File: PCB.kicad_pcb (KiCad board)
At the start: 2 copper layers, 85 x 156.5 mm, 29 parts, among them J1 Conn_01x04, J2 Screw_Terminal_01x02, J3 Screw_Terminal_01x05, J4 Screw_Terminal_01x05, K1 G5LE-1A_DC3, K2 G5LE-1A_DC3, K3 G5LE-1, K4 G5LE-1, K6 G5LE-1, K7 G5LE-1A_DC3, Q1 DMN65D8L-7, Q2 DMN65D8L-7, Q3 DMN65D8L-7, SW2 SW_SPDT, SW3 Local DI2 (decspeed), SW4 local DI0 (onoff), SW5 Local DI1 (incspeed), U1 WeMos_D1_mini

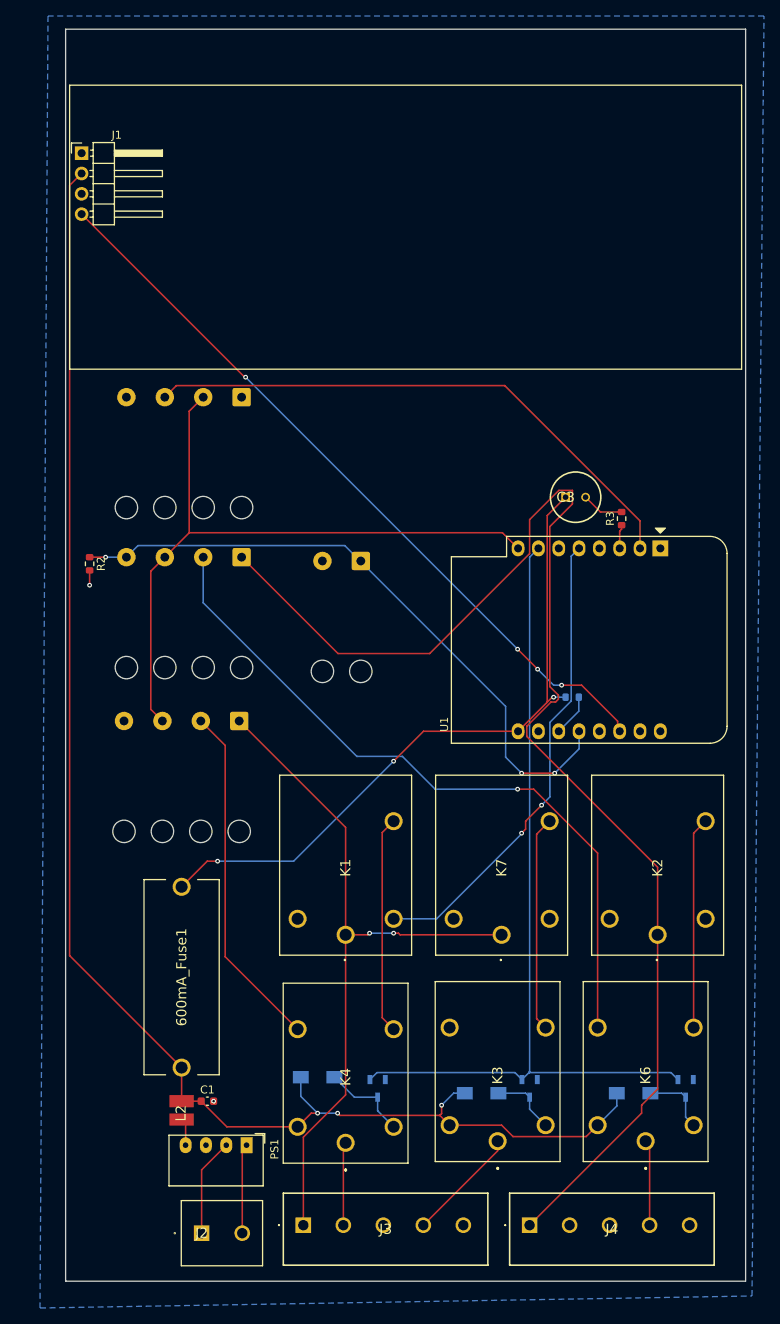
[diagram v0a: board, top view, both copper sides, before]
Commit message: remove the lots of vias so the layout is cleaner
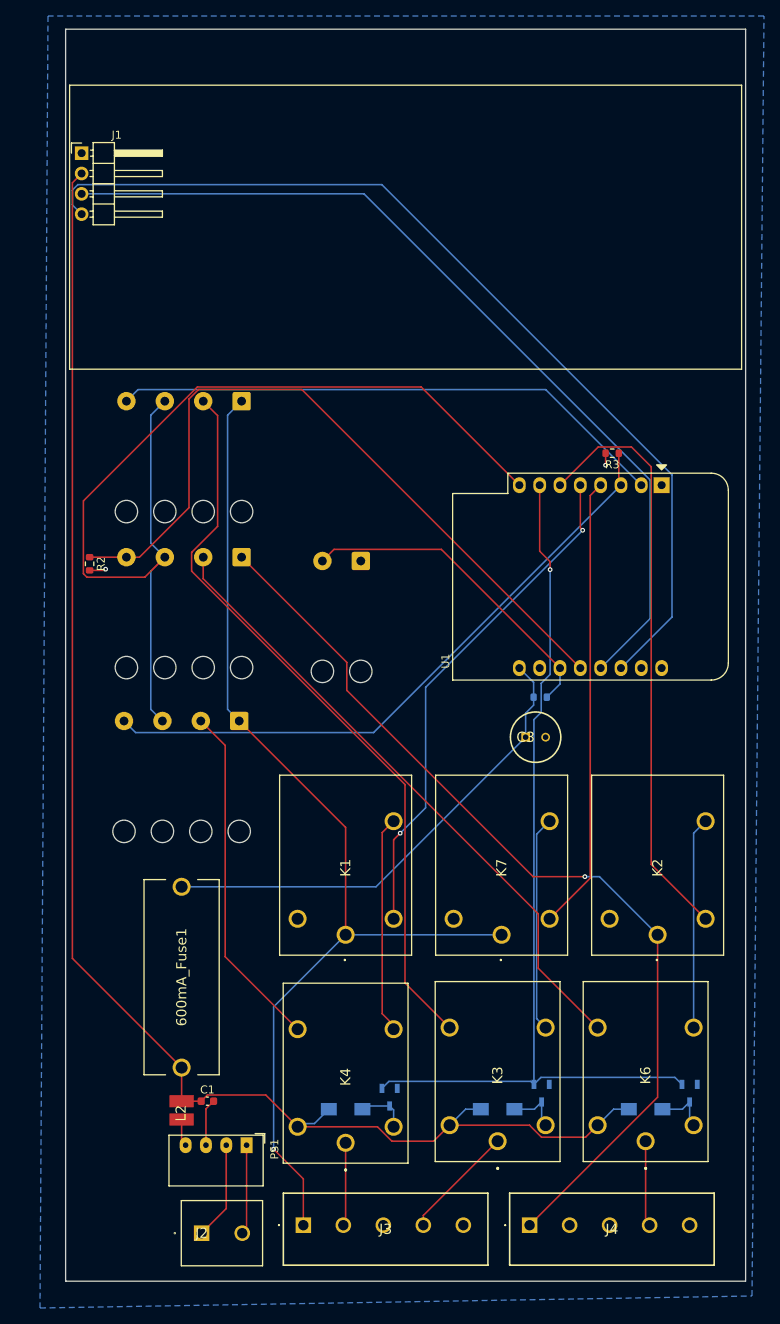
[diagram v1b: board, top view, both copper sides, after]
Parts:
- removed SW4: local DI0 (onoff), Connector_Wire:SolderWire-0.5sqmm_1x04_P4.8mm_D0.9mm_OD2.3mm_Relief
- added SW1: Local DI0 (onoff), Connector_Wire:SolderWire-0.5sqmm_1x04_P4.8mm_D0.9mm_OD2.3mm_Relief, B.Cu at (85.5, 111.5)
- SW2: value SW_SPDT -> local/remote switch
- moved C3 30.4 mm to (121.0, 153.5)
- moved R3 8.26 mm to (131.8, 118.0), turned to 180 degrees
- moved U1 7.90 mm to (138.0, 122.0)
- moved D2 5.32 mm to (98.5, 200.0)
- moved R1 4.00 mm to (122.8, 148.5)
- moved D1 2.83 mm to (117.5, 200.0)
- moved D3 2.50 mm to (136.0, 200.0)
- moved Q2 1.86 mm to (104.0, 198.5)
- moved Q1 1.62 mm to (123.0, 198.0)
- moved Q3 0.78 mm to (141.5, 198.0)
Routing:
- net SDA: track 0.00 -> 111.9 mm
- net local DI0: track 0.00 -> 93.8 mm
- net DO0: track 3.00 -> 79.6 mm
- net DO7: track 0.00 -> 73.7 mm
- net DO5: track 0.00 -> 56.8 mm
- net J4 24V: track 166.1 -> 116.5 mm, vias 0 -> 1
- net J3 24V: track 90.4 -> 134.6 mm, vias 2 -> 1
- net MCU 3V3: track 85.7 -> 128.7 mm
- net Net-(SW2-B): track 5.30 -> 40.8 mm
- net SCL: track 94.6 -> 120.5 mm, vias 4 -> 0
- net Net-(C3-+): track 84.4 -> 60.5 mm, vias 3 -> 0
- net DO3: track 80.7 -> 92.4 mm, vias 3 -> 0
- net local DI2: track 89.8 -> 79.2 mm, vias 1 -> 0
- net DO8: track 106.0 -> 115.0 mm, vias 0 -> 1
- net DO6: track 59.1 -> 64.1 mm
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
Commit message: update the pcb silkscreen names and start widening paths
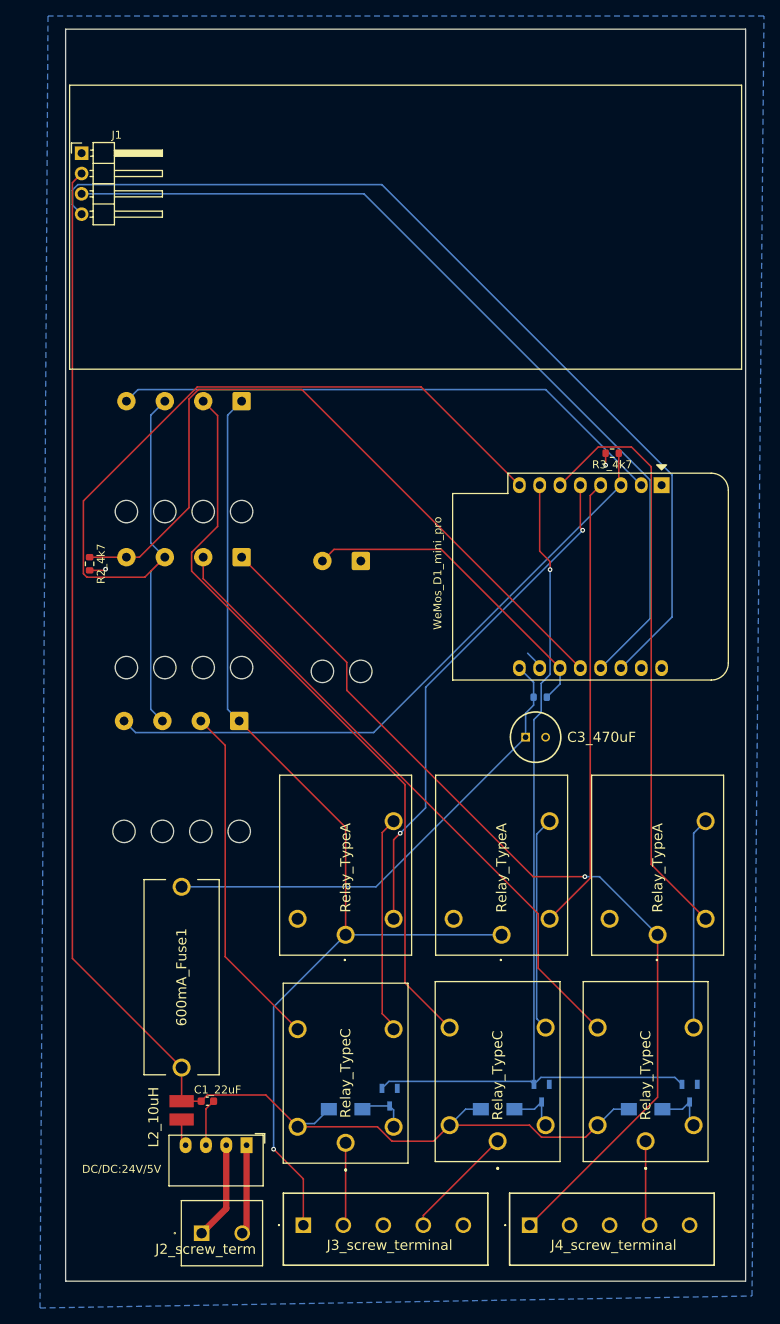
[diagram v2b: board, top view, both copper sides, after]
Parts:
- renumbered C1 to C1_22uF, C3 to C3_470uF, D1 to D1_Schottky, D2 to D2_Schottky, D3 to D3_Schottky, PS1 to DC/DC:24V/5V, J2 to J2_screw_term, J3 to J3_screw_terminal, J4 to J4_screw_terminal, L2 to L2_10uH, Q1 to Q1_MOSFET, Q2 to Q2_MOSFET, Q3 to Q3_MOSFET, R1 to R1_4k7, R2 to R2_4k7, R3 to R3_4k7, K7 to Relay_TypeA, K2 to Relay_TypeA, K1 to Relay_TypeA, K4 to Relay_TypeC, K3 to Relay_TypeC, K6 to Relay_TypeC, U1 to WeMos_D1_mini_pro
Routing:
- net GND: track 9.46 -> 11.9 mm
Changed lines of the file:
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@@
 		(descr "1729128")
 		(tags "Connector")
-		(property "Reference" "J2"
-			(at 0 0 0)
+		(property "Reference" "J2_screw_term"
+			(at 0.5 2 0)
 			(layer "F.SilkS")
 			(effects
@@
 		(descr "Resistor SMD 0603 (1608 Metric), square (rectangular) end terminal, IPC_7351 nominal, (Body size source: IPC-SM-782 page 72, https://www.pcb-3d.com/wordpress/wp-content/uploads/ipc-sm-782a_amendment_1_and_2.pdf), generated with kicad-footprint-generator")
 		(tags "resistor")
-		(property "Reference" "R3"
-			(at 0 -1.43 360)
+		(property "Reference" "R3_4k7"
+			(at 0 -1.43 0)
 			(layer "F.SilkS")
 			(effects
@@
 		)
 		(property "Value" "4k7"
-			(at 0 1.43 360)
+			(at 0 1.43 0)
 			(layer "F.Fab")
 			(effects
@@
 		)
 		(fp_text user "${REFERENCE}"
-			(at 0 0 360)
+			(at 0 0 0)
 			(layer "F.Fab")
 			(effects
@@
 		(descr "G5LE-1-DC3-1")
 		(tags "Relay or Contactor")
-		(property "Reference" "K4"
-			(at 8.225 0 90)
+		(property "Reference" "Relay_TypeC"
+			(at 8.7 0 90)
 			(layer "F.SilkS")
 			(effects
@@
 		)
 		(fp_text user "${REFERENCE}"
-			(at 8.225 0 90)
+			(at 8.7 0 90)
 			(layer "F.Fab")
 			(effects
@@
 		(descr "16-pin module, column spacing 22.86 mm (900 mils), https://wiki.wemos.cc/products:d1:d1_mini, https://c1.staticflickr.com/1/734/31400410271_f278b087db_z.jpg")
 		(tags "ESP8266 WiFi microcontroller")
-		(property "Reference" "U1"
-			(at 22 27 90)
+		(property "Reference" "WeMos_D1_mini_pro"
+			(at 11 28 90)
 			(layer "F.SilkS")
 			(effects
@@
 		)
 		(fp_text user "${REFERENCE}"
-			(at 11.43 10 90)
+			(at 11.43 10 180)
 			(layer "F.Fab")
 			(effects
@@
 		(descr "8200")
 		(tags "Inductor")
-		(property "Reference" "L2"
-			(at -0.37162 -0.07824 90)
+		(property "Reference" "L2_10uH"
+			(at -0.855 -3.5 90)
 			(layer "F.SilkS")
 			(effects
@@
 		)
 		(fp_text user "${REFERENCE}"
-			(at -0.37162 -0.07824 90)
+			(at -0.855 -3.5 90)
 			(layer "F.Fab")
 			(effects
@@
 		(descr "G5LE-1A4-DC5-4")
 		(tags "Relay or Contactor")
-		(property "Reference" "K7"
+		(property "Reference" "Relay_TypeA"
 			(at 8.375 0 90)
 			(layer "F.SilkS")
@@
 		(descr "6.3*11")
 		(tags "Capacitor Polarised")
-		(property "Reference" "C3"
-			(at 0 0 0)
+		(property "Reference" "C3_470uF"
+			(at 9.5 0 0)
 			(layer "F.SilkS")
 			(effects
@@
 		(descr "G5LE-1A4-DC5-4")
 		(tags "Relay or Contactor")
-		(property "Reference" "K2"
+		(property "Reference" "Relay_TypeA"
 			(at 8.375 0 90)
 			(layer "F.SilkS")
@@
 		(descr "1935190-1")
 		(tags "Connector")
-		(property "Reference" "J4"
-			(at 10.285 0.5 0)
+		(property "Reference" "J4_screw_terminal"
+			(at 10.5 2.5 0)
 			(layer "F.SilkS")
 			(effects
@@
 		)
 		(fp_text user "${REFERENCE}"
-			(at 10.285 0.5 0)
+			(at 10.5 2.5 0)
 			(layer "F.Fab")
 			(effects
@@
 		(descr "G5LE-1A4-DC5-4")
 		(tags "Relay or Contactor")
-		(property "Reference" "K1"
+		(property "Reference" "Relay_TypeA"
 			(at 8.375 0 90)
 			(layer "F.SilkS")
@@
 		(descr "Resistor SMD 0603 (1608 Metric), square (rectangular) end terminal, IPC_7351 nominal, (Body size source: IPC-SM-782 page 72, https://www.pcb-3d.com/wordpress/wp-content/uploads/ipc-sm-782a_amendment_1_and_2.pdf), generated with kicad-footprint-generator")
 		(tags "resistor")
-		(property "Reference" "R2"
+		(property "Reference" "R2_4k7"
 			(at 0 -1.43 90)
 			(layer "F.SilkS")
@@
 		(descr "Capacitor SMD 0603 (1608 Metric), square (rectangular) end terminal, IPC_7351 nominal, (Body size source: IPC-SM-782 page 76, https://www.pcb-3d.com/wordpress/wp-content/uploads/ipc-sm-782a_amendment_1_and_2.pdf), generated with kicad-footprint-generator")
 		(tags "capacitor")
-		(property "Reference" "C1"
-			(at 0 -1.43 0)
+		(property "Reference" "C1_22uF"
+			(at 1.275 -1.43 0)
 			(layer "F.SilkS")
 			(effects
@@
 		(descr "G5LE-1-DC3-1")
 		(tags "Relay or Contactor")
-		(property "Reference" "K3"
+		(property "Reference" "Relay_TypeC"
 			(at 8.225 0 90)
 			(layer "F.SilkS")
@@
 		(descr "http://power.murata.com/data/power/ncl/kdc_cre1.pdf")
 		(tags "murata dc-dc transformer")
-		(property "Reference" "PS1"
-			(at 0.5 -3.5 90)
+		(property "Reference" "DC/DC:24V/5V"
+			(at 3 15.62 360)
 			(layer "F.SilkS")
 			(effects
@@
 		(descr "G5LE-1-DC3-1")
 		(tags "Relay or Contactor")
-		(property "Reference" "K6"
+		(property "Reference" "Relay_TypeC"
 			(at 8.225 0 90)
 			(layer "F.SilkS")
@@
 		(descr "1935190-1")
 		(tags "Connector")
-		(property "Reference" "J3"
-			(at 10.285 0.5 0)
+		(property "Reference" "J3_screw_terminal"
+			(at 10.785 2.5 0)
 			(layer "F.SilkS")
 			(effects
@@
 		)
 		(fp_text user "${REFERENCE}"
-			(at 10.285 0.5 0)
+			(at 10.785 2.5 0)
 			(layer "F.Fab")
 			(effects
@@
 		(descr "DMN65D8L-7")
 		(tags "MOSFET (N-Channel)")
-		(property "Reference" "Q3"
-			(at 0 0 90)
+		(property "Reference" "Q3_MOSFET"
+			(at 0 -3 90)
 			(layer "B.SilkS")
 			(effects
@@
 		)
 		(fp_text user "${REFERENCE}"
-			(at 0 0 90)
+			(at 0 -3 90)
 			(layer "B.Fab")
 			(effects
@@
 		(descr "DMN65D8L-7")
 		(tags "MOSFET (N-Channel)")
-		(property "Reference" "Q2"
-			(at 0 0 90)
+		(property "Reference" "Q2_MOSFET"
+			(at 0 -3 90)
 			(layer "B.SilkS")
 			(effects
@@
 		)
 		(fp_text user "${REFERENCE}"
-			(at 0 0 90)
+			(at 0 -3 90)
 			(layer "B.Fab")
 			(effects
@@
 		(descr "DMN65D8L-7")
 		(tags "MOSFET (N-Channel)")
-		(property "Reference" "Q1"
-			(at 0 0 90)
+		(property "Reference" "Q1_MOSFET"
+			(at 0 -2 90)
 			(layer "B.SilkS")
 			(effects
@@
 		)
 		(fp_text user "${REFERENCE}"
-			(at 0 0 90)
+			(at 0 -2 90)
 			(layer "B.Fab")
 			(effects
@@
 		(descr "Resistor SMD 0603 (1608 Metric), square (rectangular) end terminal, IPC_7351 nominal, (Body size source: IPC-SM-782 page 72, https://www.pcb-3d.com/wordpress/wp-content/uploads/ipc-sm-782a_amendment_1_and_2.pdf), generated with kicad-footprint-generator")
 		(tags "resistor")
-		(property "Reference" "R1"
+		(property "Reference" "R1_4k7"
 			(at 0 1.43 0)
 			(layer "B.SilkS")
@@
 		)
 		(fp_text user "${REFERENCE}"
-			(at 0 0 0)
+			(at 2.675 -0.25 0)
 			(layer "B.Fab")
 			(effects
@@
 		(descr "SMA~DO-214AC")
 		(tags "Schottky Diode")
-		(property "Reference" "D2"
-			(at 0 0 0)
+		(property "Reference" "D2_Schottky"
+			(at -2 -2.5 0)
 			(layer "B.SilkS")
 			(effects
@@
 		(descr "SMA~DO-214AC")
 		(tags "Schottky Diode")
-		(property "Reference" "D3"
-			(at 0 0 0)
+		(property "Reference" "D3_Schottky"
+			(at -2.5 -2.5 0)
 			(layer "B.SilkS")
 			(effects
@@
 		(descr "SMA~DO-214AC")
 		(tags "Schottky Diode")
-		(property "Reference" "D1"
-			(at 0 0 0)
+		(property "Reference" "D1_Schottky"
+			(at -2 -2.5 0)
 			(layer "B.SilkS")
 			(effects
@@
 	)
 	(segment
-		(start 80.45 199)
-		(end 80.5 199)
-		(width 0.2)
-		(layer "F.Cu")
-		(net 1)
-	)
-	(segment
 		(start 121.484745 202)
 		(end 122.984745 203.5)
@@
 	)
 	(segment
+		(start 122.76 144.86)
+		(end 122.76 144.51)
+		(width 0.2)
+		(layer "B.Cu")
+		(net 2)
+	)
+	(segment
+		(start 122.76 144.51)
+		(end 121.25 143)
+		(width 0.2)
+		(layer "B.Cu")
+		(net 2)
+	)
+	(segment
 		(start 86.12 214.96)
 		(end 85.58 215.5)
@@
 		(start 86.12 204.5)
 		(end 86.12 214.96)
-		(width 0.2)
+		(width 0.8)
 		(layer "F.Cu")
 		(net 3)
@@
 		(start 83.58 204.5)
 		(end 83.58 212.42)
-		(width 0.2)
+		(width 0.8)
 		(layer "F.Cu")
 		(net 14)
@@
 		(start 83.58 212.42)
 		(end 80.5 215.5)
-		(width 0.2)
+		(width 0.8)
 		(layer "F.Cu")
 		(net 14)

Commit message: widen tracks with larger current and fix the local/remote switch footprint
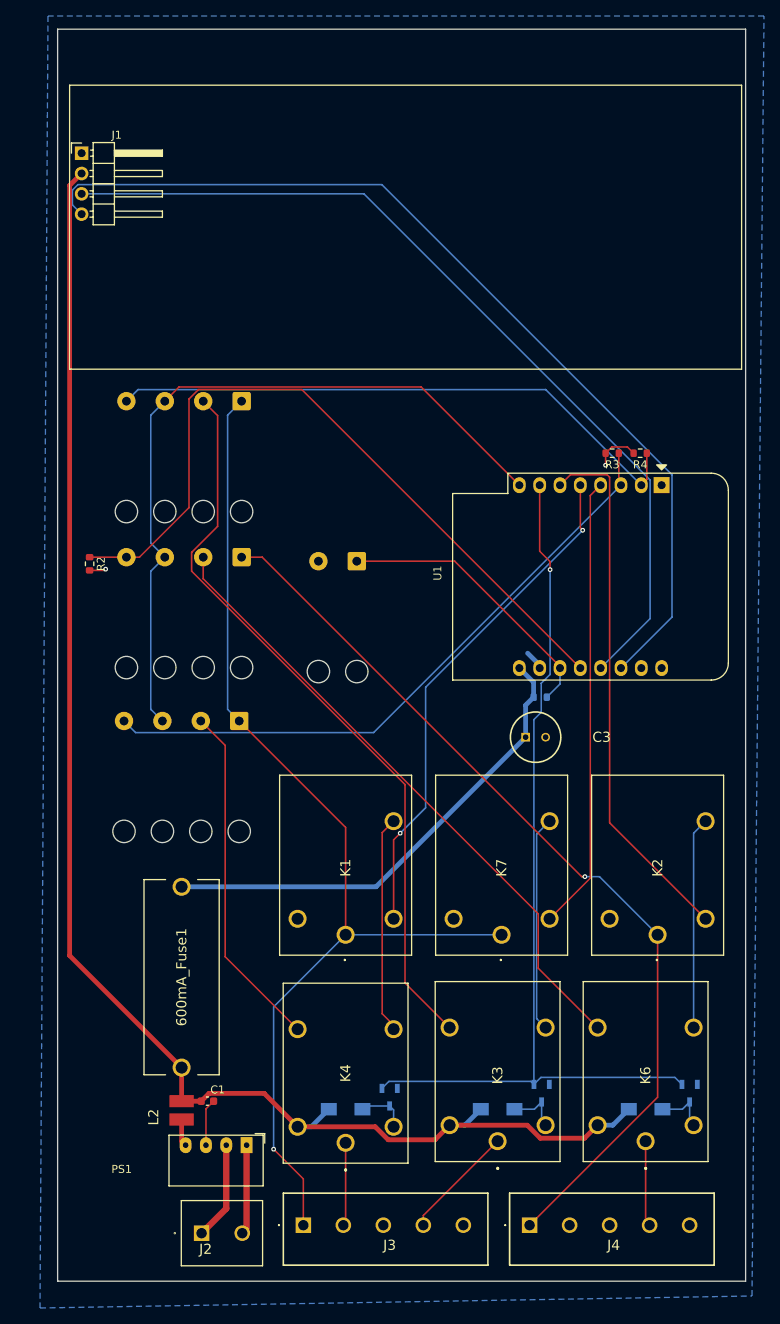
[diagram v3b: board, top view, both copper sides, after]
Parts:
- removed SW2: local/remote switch, Connector_Wire:SolderWire-0.5sqmm_1x02_P4.8mm_D0.9mm_OD2.3mm_Relief
- added R4: 4k7, Resistor_SMD:R_0603_1608Metric, F.Cu at (135.3, 118.0)
- added SW4: local/remote switch, Connector_Wire:SolderWire-0.5sqmm_1x02_P4.8mm_D0.9mm_OD2.3mm_Relief, B.Cu at (99.9, 131.5)
- renumbered C1_22uF to C1, C3_470uF to C3, D1_Schottky to D1, D2_Schottky to D2, D3_Schottky to D3, J2_screw_term to J2, J3_screw_terminal to J3, J4_screw_terminal to J4, Relay_TypeA to K1, Relay_TypeA to K2, Relay_TypeC to K3, Relay_TypeC to K4, Relay_TypeC to K6, Relay_TypeA to K7, L2_10uH to L2, DC/DC:24V/5V to PS1, Q1_MOSFET to Q1, Q2_MOSFET to Q2, Q3_MOSFET to Q3, R1_4k7 to R1, R2_4k7 to R2, R3_4k7 to R3, WeMos_D1_mini_pro to U1
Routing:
- net MCU 3V3: track 128.7 -> 92.9 mm
- net DO7: track 73.7 -> 67.0 mm
- net Net-(SW4-A): track 40.8 -> 35.4 mm
- net DOA: track 69.9 -> 74.2 mm
- net GND: track 11.9 -> 16.1 mm
- net J4 24V: track 116.5 -> 114.5 mm
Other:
- board size 85 x 156.5 mm -> 86 x 156.5 mm

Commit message: start improving the pcb schematic as per feedback no 2
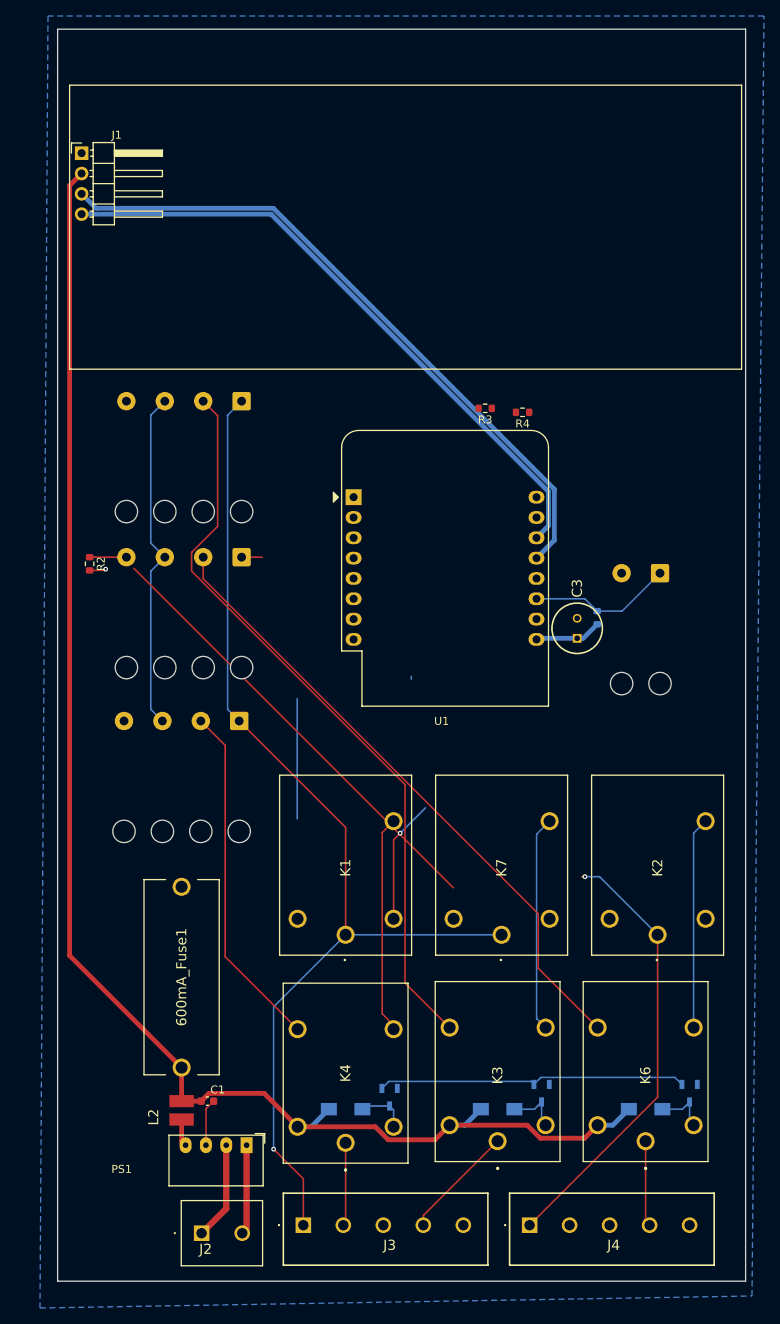
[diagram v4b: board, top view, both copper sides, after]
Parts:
- moved U1 38.5 mm to (99.5, 123.5), turned to 0 degrees
- moved SW4 37.9 mm to (137.8, 133.0)
- moved R3 16.8 mm to (115.9, 112.4)
- moved R4 15.6 mm to (120.6, 112.9)
- moved C3 13.9 mm to (127.4, 141.1), turned to 90 degrees
- moved R1 12.2 mm to (129.9, 138.6), turned to 90 degrees
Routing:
- net DO3: track 92.4 -> 4.60 mm
- net DO0: track 79.6 -> 0.00 mm
- net DO8: track 115.0 -> 38.7 mm, vias 1 -> 0
- net DOA: track 74.2 -> 0.00 mm
- net DO7: track 67.0 -> 0.00 mm
- net DO5: track 56.8 -> 0.00 mm
- net Net-(C3-+): track 60.5 -> 8.37 mm
- net MCU 3V3: track 92.9 -> 42.8 mm
- net SCL: track 120.5 -> 79.1 mm
- net DO6: track 64.1 -> 30.6 mm, vias 2 -> 1
- net SDA: track 111.9 -> 83.9 mm
- net Net-(SW4-A): track 35.4 -> 18.0 mm
- net GND: track 16.1 -> 8.31 mm, vias 2 -> 1
